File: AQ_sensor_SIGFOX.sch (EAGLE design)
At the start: 49 parts, among them IC2 MCP73831/OT, J1 F-1X03-SIP-100-32, SW1 PCM12SMTR, SW2 PCM12SMTR, U2 TEXAS_INSTRUMENTS_SN74HC125TE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, U3 TEXAS_INSTRUMENTS_LM1117IMP-3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, X1 53048-08, X2 SIMLOCK-C707_10M006_512_2, X4 50 Ohms

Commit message: Added sigfox circuit
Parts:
- removed C10: 33pF, rcl:C-EUC0603
- removed C11: 10pF, rcl:C-EUC0603
- removed C4: 10uF, rcl:C-EUC0603
- removed C9: 100uF, rcl:CPOL-EUD
- removed CHRG, PWR: RED, led:LEDCHIP-LED0603
- removed CN1: (no value), AQ_sensor_GSM:JST_2PIN-SMT-RA
- removed D1, D4: ON_SEMI_1N4148WSON_SEMI_1N4148WS_0_0, AQ_sensor_GSM:ON_SEMI_1N4148WSON_SEMI_1N4148WS_0_0
- removed D2: ON_SEMICONDUCTOR_MMSZ5231BT1GON_SEMICONDUCTOR_MMSZ5231BT1G_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, AQ_sensor_GSM:ON_SEMICONDUCTOR_MMSZ5231BT1GON_SEMICONDUCTOR_MMSZ5231BT1G_0_0
- removed D3: SEMTECH_SMF05CSEMTECH_SMF05C_0_0, AQ_sensor_GSM:SEMTECH_SMF05CSEMTECH_SMF05C_0_0
- removed FULL, NET: YELLOW, led:LEDCHIP-LED0603
- removed IC2: MCP73831/OT, AQ_sensor_GSM:MCP73831/OT
- removed R1, R17, R19, R6, R7: 470, rcl:R-EU_R0603
- removed R20: 2K, rcl:R-EU_R0603
- removed RI: ORANGE, led:LEDCHIP-LED0603
- removed S1: KMR621NGLFS, AQ_sensor_GSM:KMR621NGLFS
- removed TP1, TP2: TPB1,27, testpad:TPB1,27
- removed U1: (no value), AQ_sensor_GSM:GSM_SIM800L
- removed U2: TEXAS_INSTRUMENTS_SN74HC125TEXAS_INSTRUMENTS_SN74HC125_0_0, AQ_sensor_GSM:TEXAS_INSTRUMENTS_SN74HC125TEXAS_INSTRUMENTS_SN74HC125_0_0
- removed X2: SIMLOCK-C707_10M006_512_2, AQ_sensor_GSM:SIMLOCK-C707_10M006_512_2
- removed X4: 50 Ohms, AQ_sensor_GSM:SMACONNECTOR_EDGE_UFL
- added C2: 100pF, rcl:C-EUC0603
- added C3, C5: 100nF, rcl:C-EUC0603
- added L1: 47NH, OPL_Inductor:SMD-INDUCTOR-2.2UH-20%-1.2A(0805)
- added R10, R8, R9: 470, rcl:R-EU_R0603
- added R2: 0R, rcl:R-EU_R0603
- added R3: 100K 1/16W, rcl:R-EU_R0603
- added RADIO_LED: ORANGE, led:LEDCHIP-LED0603
- added RX_LED, TX_LED: GREEN, led:LEDCHIP-LED0603
- added U$1: WSSFM10RWSSFM10R2R4, WisolWSSFM10R:WSSFM10RWSSFM10R2R4
- added X3: (no value), AQ_sensor_GSM:SMACONNECTOR_EDGE_UFL
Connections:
- removed net 1.8V: D3.1_CATHODE, TP1.TP, U1.VSIM, X2.1
- removed net 2.8V: TP2.TP, U1.VEXT
- removed net GSM_ANT: U1.ANT, X4.ANT
- removed net GSM_RST: U1.RESET
- removed net GSM_RST_O: SV1.5
- removed net GSM_RX: D4.ANODE, U1.UART_RXD
- removed net GSM_RX_O: D4.CATHODE, SV1.8
- removed net GSM_TX: U1.UART_TXD, U2B.2A
- removed net GSM_TX_5V: SV1.7, U2B.2Y
- removed net N$10: NET.A, R6.2
- removed net N$11: PWR.A, R7.2
- removed net N$12: FULL.A, R19.1
- removed net N$13: IC2.PROG, R20.1
- removed net N$14: R1.2, RI.A
- removed net N$6: CHRG.C, R17.1
- removed net N$9: IC2.STAT, R17.2, R19.2
- removed net NETSTAT: U1.NETLIGHT, U2A.1A
- removed net NETSTAT_5V: R6.1, U2A.1Y
- removed net PWRKEY: D1.ANODE, S1.2, U1.PWRKEY
- removed net PWRSTAT: U1.STATUS, U2C.3A
- removed net PWRSTAT_5V: R7.1, U2C.3Y
- removed net RI: U1.UART_RI, U2D.4A
- removed net RI_5V: RI.C, U2D.4Y
- removed net SIMCLK: D3.2_CATHODE, U1.SIM_CLK, X2.3
- removed net SIMDATA: D3.3_CATHODE, U1.SIM_DATA, X2.6
- removed net SIMRST: D3.4_CATHODE, U1.SIM_RST, X2.2
- removed net VRTC: C4.1, U1.VRTC
- removed net V_LIPO: C10.1, C11.1, C9.+, CN1.2, D2.K, IC2.VBAT, U1.VBAT
- new net N$1: C2.1, U$1.30
- new net N$15: R8.2, TX_LED.A
- new net N$2: C2.2, L1.1, R2.2
- new net N$3: R2.1, X3.ANT
- new net N$5: C5.1, R3.2, U$1.19
- new net N$7: R10.2, RADIO_LED.A
- new net N$8: R9.2, RX_LED.A
- new net RADIO_LED: R10.1, U$1.RADIOLED
- new net RX_LED: R9.1, U$1.RXLED/DBG_DATA
- new net TX_LED: R8.1, U$1.TXLED_DBG_CLK
- new net WISOL_RX: SV1.8, U$1.UARTRX
- new net WISOL_TX: SV1.7, U$1.UARTTX
- new net WISON_RST: U$1.GPIO9
- net +3V3: now also C3.1, R3.1, U$1.21
- net +5V: no longer CHRG.A, IC2.VDD, R1.1, U2E.VCC
- net GND: now also C3.2, C5.2, L1.2, RADIO_LED.C, RX_LED.C, TX_LED.C, U$1.1, U$1.2, U$1.20, U$1.28, U$1.29, U$1.3, U$1.31, U$1.4, X3.GND1, X3.GND2, X3.GND3, X3.GND4; no longer C10.2, C11.2, C4.2, C9.-, CN1.1, D1.CATHODE, D2.A, D3.ANODE, FULL.C, IC2.VSS, NET.C, PWR.C, R20.2, S1.1, U1.GND, U2A.1_!OE!, U2B.4_!OE!, U2C.2_!OE!, U2D.3_!OE!, U2E.GND, X2.4, X4.GND1, X4.GND2, X4.GND3, X4.GND4
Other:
- note added: "Note: This library was designed"
- note added: "PCB components remain the same."
- note added: "Recommended by Wisol"
- note added: "WSSFM10R H/W Design Guide"
- note added: "and R# have a shorter footprint (the"
- note added: "for Wisol WSSFM10R2 Aand R4, which"
- note added: "has a longer footprint. Wisol WSSFM10R1"
- note added: "sensors.AFRICA_AQ_SENSOR"
- note added: "top part is trancated). All pins and"
- note removed: "CHARGING CIRCUIT"
- note removed: "DECOUPLING CIRCUIT"
- note removed: "GSM ANTENNA"
- note removed: "LEVEL SHIFTER"
- note removed: "LIPO BATTERY"
- note removed: "POWER KEY"
- note removed: "SIM CARD HOLDER"
- note removed: "SIM800H"
- note removed: "STATUS LEDS"
- note removed: "TEST PADS"
- note removed: "sensors.AFRICA MRC"

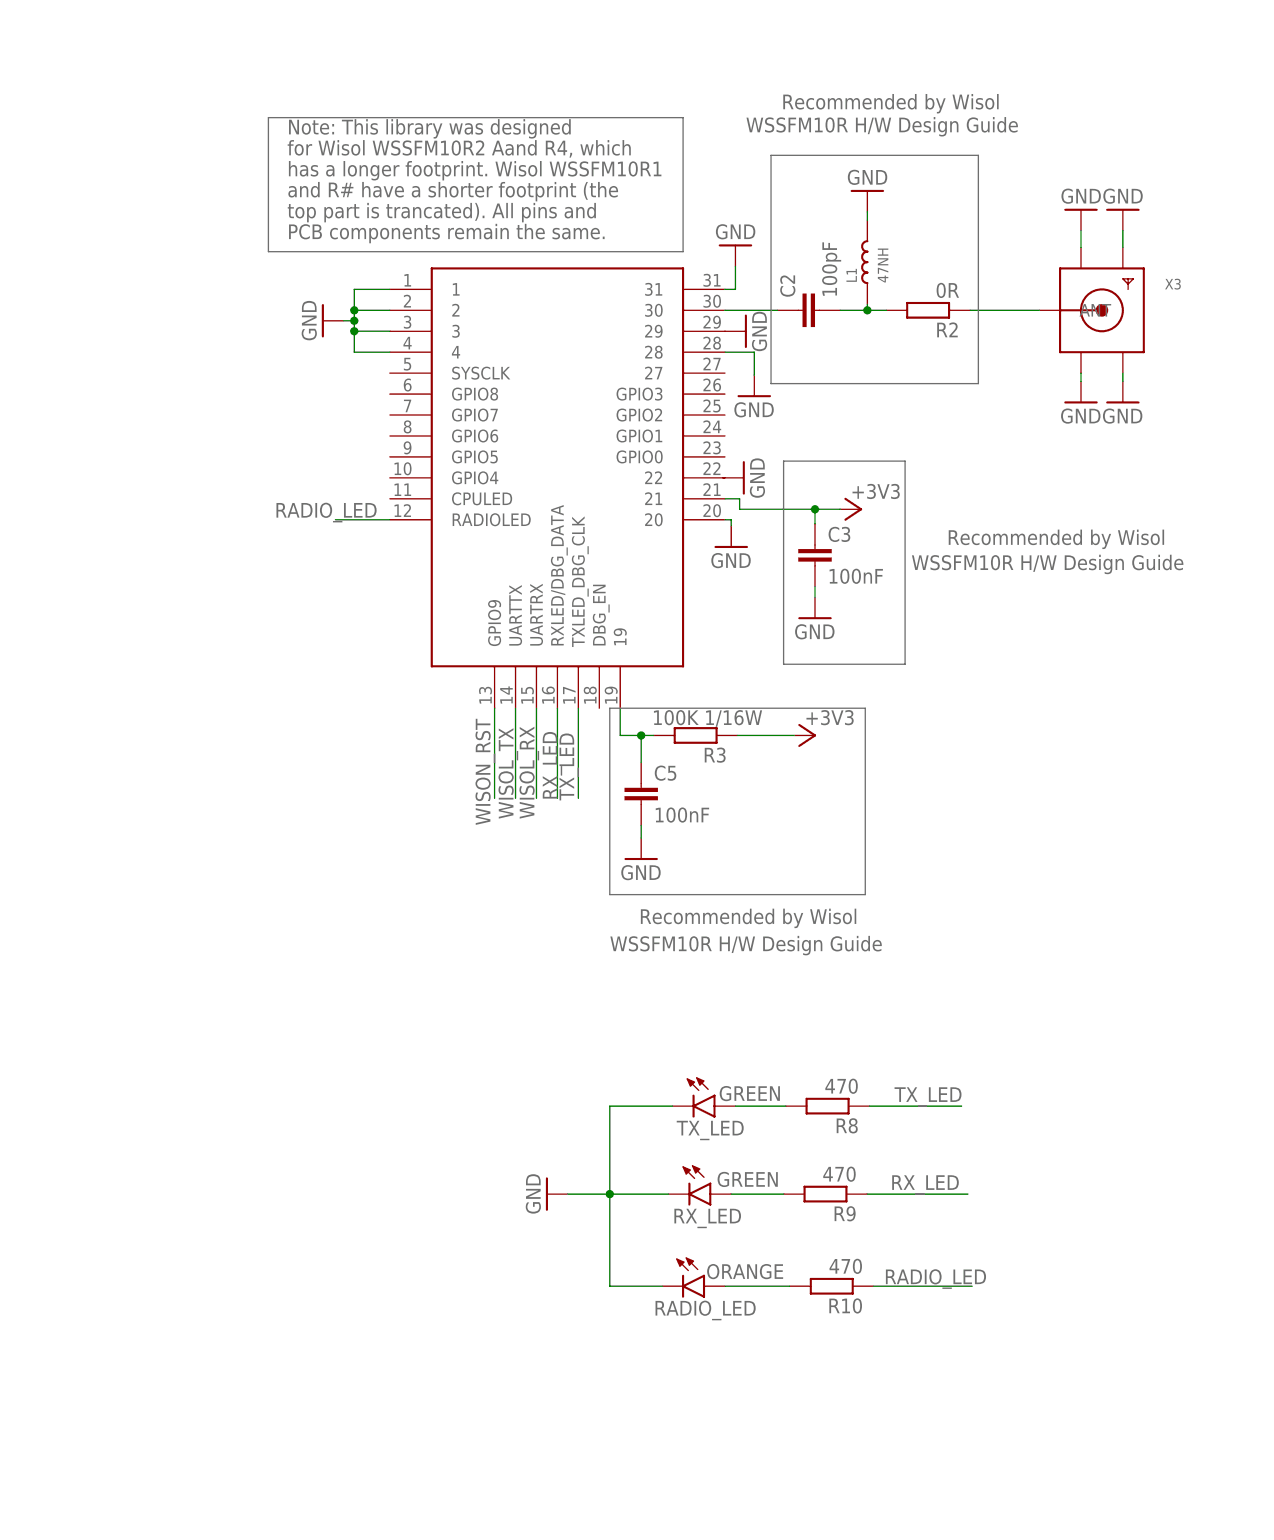
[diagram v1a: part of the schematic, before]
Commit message: Changed DHT power from 5V to 3v3
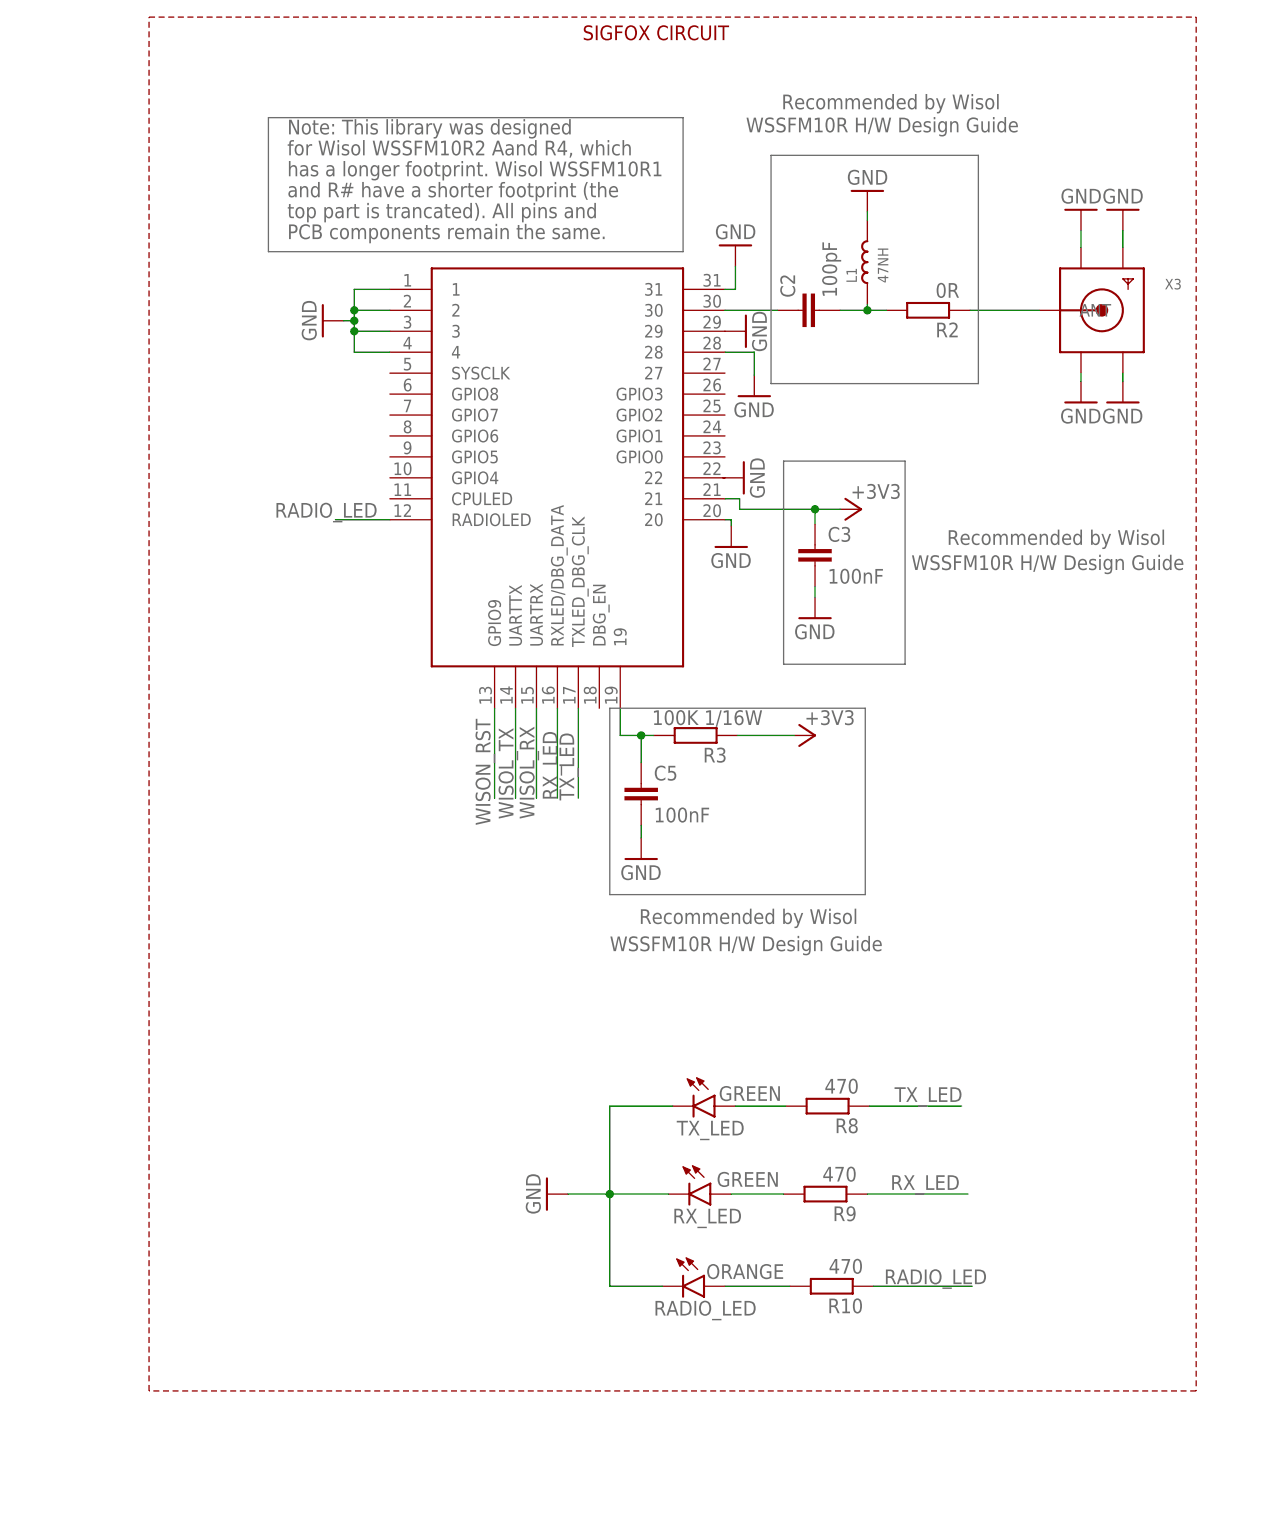
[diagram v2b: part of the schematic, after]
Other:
- note added: "SIGFOX CIRCUIT"
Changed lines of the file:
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@@
 <text x="306.578" y="141.986" size="1.778" layer="95">WSSFM10R H/W Design Guide</text>
 <text x="310.134" y="145.288" size="1.778" layer="95">Recommended by Wisol</text>
+<wire x1="377.698" y1="255.27" x2="377.698" y2="88.646" width="0.1524" layer="94" style="shortdash"/>
+<wire x1="377.698" y1="88.646" x2="250.698" y2="88.646" width="0.1524" layer="94" style="shortdash"/>
+<wire x1="250.698" y1="88.646" x2="250.698" y2="255.27" width="0.1524" layer="94" style="shortdash"/>
+<wire x1="250.698" y1="255.27" x2="377.698" y2="255.27" width="0.1524" layer="94" style="shortdash"/>
+<text x="303.276" y="252.476" size="1.778" layer="94">SIGFOX CIRCUIT</text>
 </plain>
 <instances>

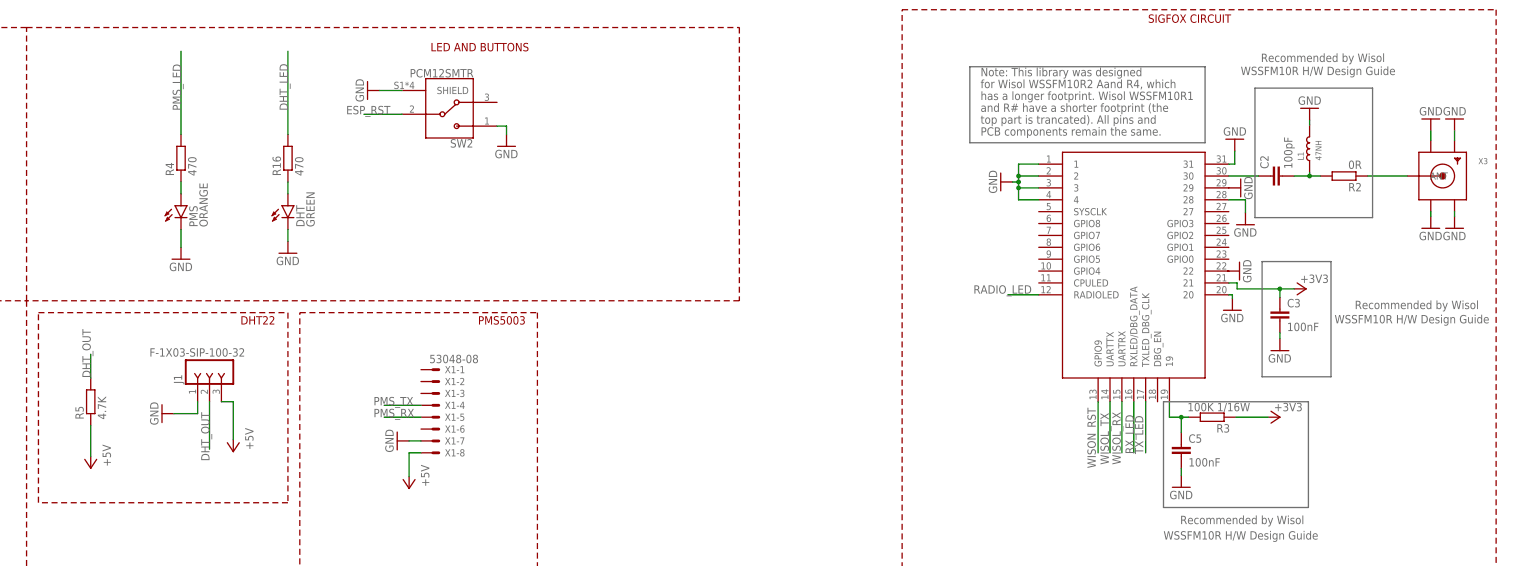
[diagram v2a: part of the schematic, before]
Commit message: added via stitching
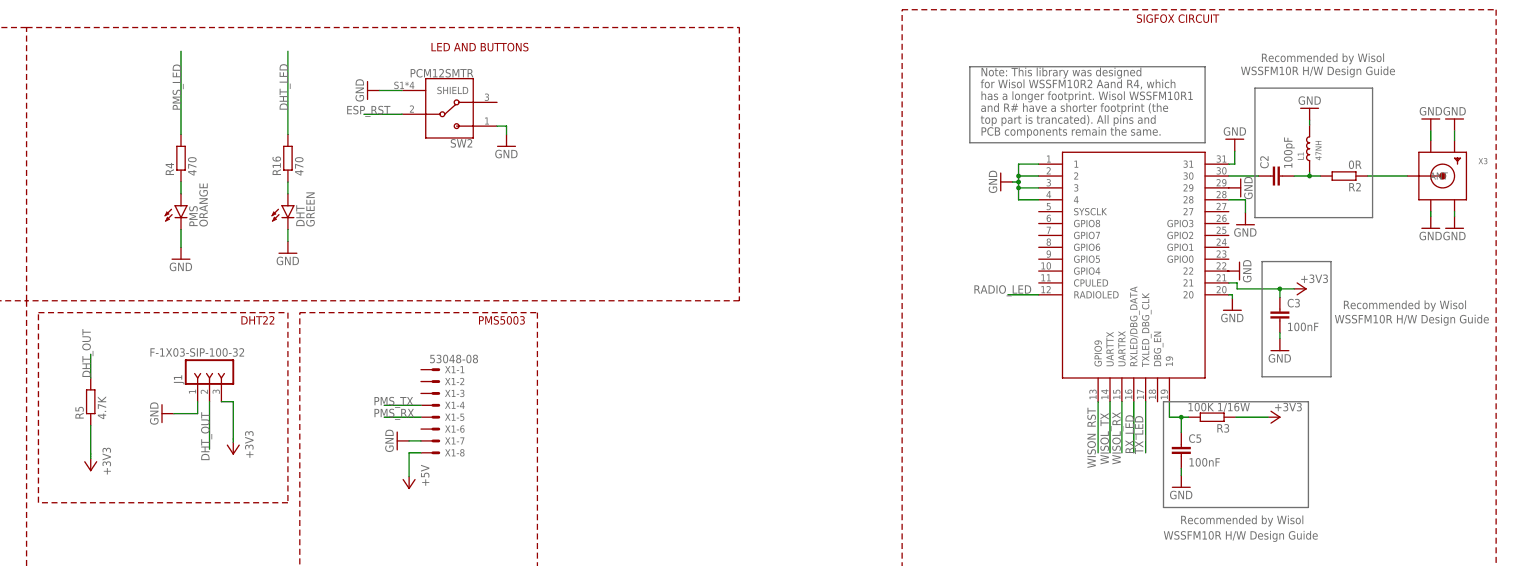
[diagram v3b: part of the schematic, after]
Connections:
- net +3V3: now also J1.3, R5.1
- net +5V: no longer J1.3, R5.1
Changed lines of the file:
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@@
 <part name="H4" library="AQ_sensor_GSM" library_urn="urn:adsk.eagle:library:30300195" deviceset="MOUNT-PAD-ROUND" device="2.8" package3d_urn="urn:adsk.eagle:package:30300289/1"/>
 <part name="GND61" library="supply1" library_urn="urn:adsk.eagle:library:371" deviceset="GND" device=""/>
-<part name="P+12" library="supply1" library_urn="urn:adsk.eagle:library:371" deviceset="+5V" device=""/>
-<part name="P+13" library="supply1" library_urn="urn:adsk.eagle:library:371" deviceset="+5V" device=""/>
 <part name="GND13" library="supply1" library_urn="urn:adsk.eagle:library:371" deviceset="GND" device=""/>
 <part name="DHT" library="led" library_urn="urn:adsk.eagle:library:259" deviceset="LED" device="CHIP-LED0603" package3d_urn="urn:adsk.eagle:package:15819/3" value="GREEN"/>
@@
 <part name="RADIO_LED" library="led" library_urn="urn:adsk.eagle:library:259" deviceset="LED" device="CHIP-LED0603" package3d_urn="urn:adsk.eagle:package:15819/3" value="ORANGE"/>
 <part name="GND35" library="supply1" library_urn="urn:adsk.eagle:library:371" deviceset="GND" device=""/>
+<part name="+3V4" library="supply1" library_urn="urn:adsk.eagle:library:371" deviceset="+3V3" device=""/>
+<part name="+3V5" library="supply1" library_urn="urn:adsk.eagle:library:371" deviceset="+3V3" device=""/>
 </parts>
 <sheets>
@@
 <wire x1="342.392" y1="176.784" x2="342.392" y2="201.422" width="0.1524" layer="95"/>
 <wire x1="342.392" y1="201.422" x2="327.66" y2="201.422" width="0.1524" layer="95"/>
-<text x="347.472" y="191.262" size="1.778" layer="95">Recommended by Wisol</text>
+<text x="344.932" y="191.262" size="1.778" layer="95">Recommended by Wisol</text>
 <text x="343.154" y="188.214" size="1.778" layer="95">WSSFM10R H/W Design Guide</text>
 <wire x1="306.578" y1="171.45" x2="337.566" y2="171.45" width="0.1524" layer="95"/>
@@
 <wire x1="250.698" y1="88.646" x2="250.698" y2="255.27" width="0.1524" layer="94" style="shortdash"/>
 <wire x1="250.698" y1="255.27" x2="377.698" y2="255.27" width="0.1524" layer="94" style="shortdash"/>
-<text x="303.276" y="252.476" size="1.778" layer="94">SIGFOX CIRCUIT</text>
+<text x="300.736" y="252.476" size="1.778" layer="94">SIGFOX CIRCUIT</text>
 </plain>
 <instances>
@@
 <attribute name="VALUE" x="24.384" y="102.87" size="1.778" layer="96"/>
 </instance>
-<instance part="P+12" gate="1" x="107.696" y="160.782" smashed="yes" rot="R180">
-<attribute name="VALUE" x="110.236" y="165.862" size="1.778" layer="96" rot="R270"/>
-</instance>
-<instance part="P+13" gate="1" x="77.216" y="157.226" smashed="yes" rot="R180">
-<attribute name="VALUE" x="79.756" y="162.306" size="1.778" layer="96" rot="R270"/>
-</instance>
 <instance part="GND13" gate="1" x="136.398" y="237.998" smashed="yes" rot="R270">
 <attribute name="VALUE" x="133.858" y="240.538" size="1.778" layer="96" rot="R270"/>
@@
 <instance part="GND35" gate="1" x="298.958" y="112.522" smashed="yes" rot="R270">
 <attribute name="VALUE" x="296.418" y="115.062" size="1.778" layer="96" rot="R270"/>
+</instance>
+<instance part="+3V4" gate="G$1" x="77.216" y="156.718" smashed="yes" rot="R180">
+<attribute name="VALUE" x="79.756" y="161.798" size="1.778" layer="96" rot="R270"/>
+</instance>
+<instance part="+3V5" gate="G$1" x="107.696" y="160.274" smashed="yes" rot="R180">
+<attribute name="VALUE" x="110.236" y="165.354" size="1.778" layer="96" rot="R270"/>
 </instance>
 </instances>
@@
 <junction x="55.88" y="22.86"/>
 </segment>
-<segment>
-<pinref part="J1" gate="G$1" pin="3"/>
-<wire x1="105.156" y1="171.45" x2="107.696" y2="171.45" width="0.1524" layer="91"/>
-<wire x1="107.696" y1="171.45" x2="107.696" y2="163.322" width="0.1524" layer="91"/>
-<pinref part="P+12" gate="1" pin="+5V"/>
-</segment>
-<segment>
-<pinref part="R5" gate="G$1" pin="1"/>
-<wire x1="77.216" y1="166.37" x2="77.216" y2="159.766" width="0.1524" layer="91"/>
-<pinref part="P+13" gate="1" pin="+5V"/>
-</segment>
 </net>
 <net name="+3V3" class="1">
@@
 <wire x1="322.072" y1="168.148" x2="328.93" y2="168.148" width="0.1524" layer="91"/>
 </segment>
+<segment>
+<pinref part="R5" gate="G$1" pin="1"/>
+<wire x1="77.216" y1="166.37" x2="77.216" y2="160.274" width="0.1524" layer="91"/>
+<pinref part="+3V4" gate="G$1" pin="+3V3"/>
+<wire x1="77.216" y1="160.274" x2="77.216" y2="159.766" width="0.1524" layer="91"/>
+<wire x1="77.216" y1="159.258" x2="77.216" y2="159.766" width="0.1524" layer="91"/>
+</segment>
+<segment>
+<pinref part="J1" gate="G$1" pin="3"/>
+<wire x1="105.156" y1="171.45" x2="107.696" y2="171.45" width="0.1524" layer="91"/>
+<wire x1="107.696" y1="171.45" x2="107.696" y2="163.576" width="0.1524" layer="91"/>
+<pinref part="+3V5" gate="G$1" pin="+3V3"/>
+<wire x1="107.696" y1="163.576" x2="107.696" y2="163.322" width="0.1524" layer="91"/>
+<wire x1="107.696" y1="162.814" x2="107.696" y2="163.322" width="0.1524" layer="91"/>
+</segment>
 </net>
